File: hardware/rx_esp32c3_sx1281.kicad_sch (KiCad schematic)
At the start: 43 parts, among them U21 SX1281IMLTRT, U22 ESP32-C3FH4, U23 TLV75533PDQNR, X2 CJ17-400001010B20

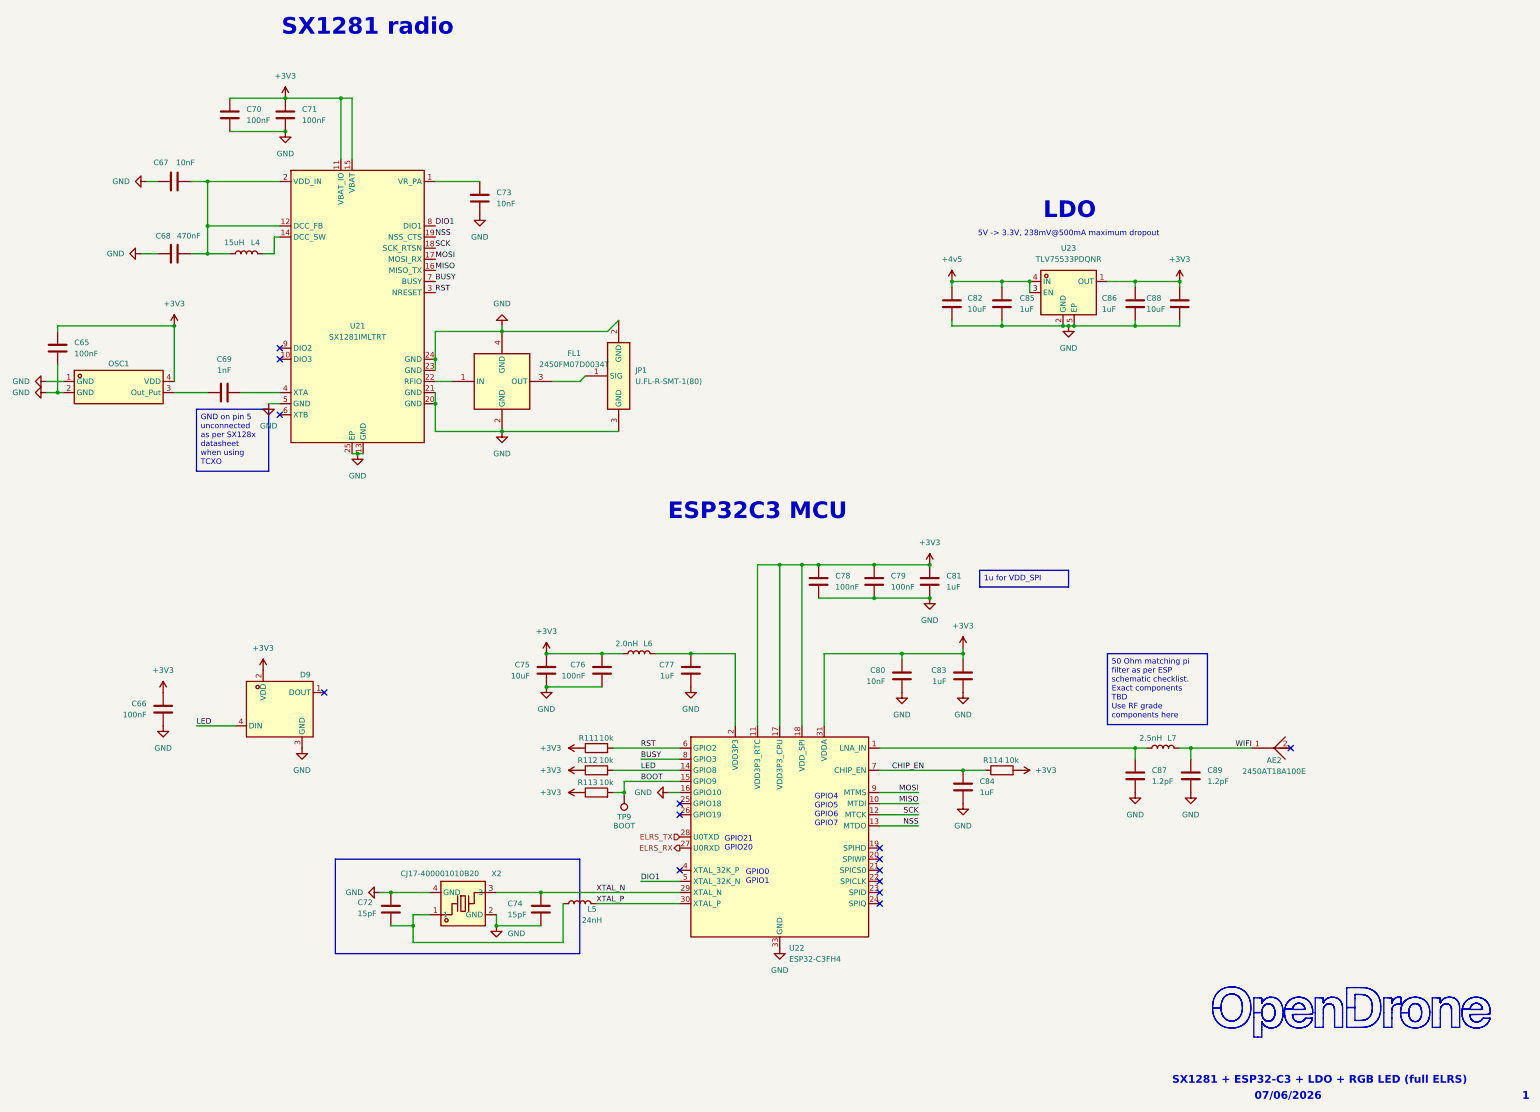
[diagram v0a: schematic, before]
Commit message: One board: merge Base and Core onto the OpenAIO-Whoop 8L HDI stackup
- hardware/OpenAIO.kicad_pcb: the routed Base and Core layouts of 8fa8d7b
  side by side in one board, all routing kept (Core promoted to 8 layers
  before the append so no Base layer was dropped). J90/J91 LGA deleted;
  their 46 nets are now direct links (51 unconnected, listed in
  research/ROUTING.md). Stackup and board setup from OpenAIO-Whoop:
  8L HDI 1+6+1, 0.997 mm, 1 oz all layers, microvia 0.25/0.10,
  buried 0.33/0.15. Base DRC severities and exclusions kept.
- hardware/OpenAIO.kicad_dru: canonical block, Whoop HDI via rules,
  Base/Core rules that still apply; LGA, 2 oz and 1.6 mm via rules gone.
- Schematic: core_interface sheet removed; DPS368 baro U28 on I2C0;
  review fixes (U3 HF cap C116, RP2354 caps C117/C118, buzzer flyback D10,
  SD card on +3.3V, D9 on +4v5, FLASH_CS -> SD_CS, PWR_FLAGs, U7 pin
  names, ESC cap pin types, L4 LCSC). ERC 32 -> 0 errors.
- Libraries project-local: every footprint, 3D model and symbol in lib;
  OPENDRONE_LIB aliases removed from the lib tables.
- Two-board projects, multiboard config and LGA tools removed; Whoop
  board tools added in hardware/tools.
- Docs: README, AGENTS.md, research/ROUTING.md (hand-over),
  SCHEMATIC-REVIEW-2026-10-15.md, Betaflight target baro.

DRC: 38 errors (25 dangling LGA escape vias, 13 Core leftovers listed),
51 unconnected (the Base-Core links), 0 net or value parity issues.

Co-Authored-By: Claude Opus 5.5 <noreply@anthropic.com>
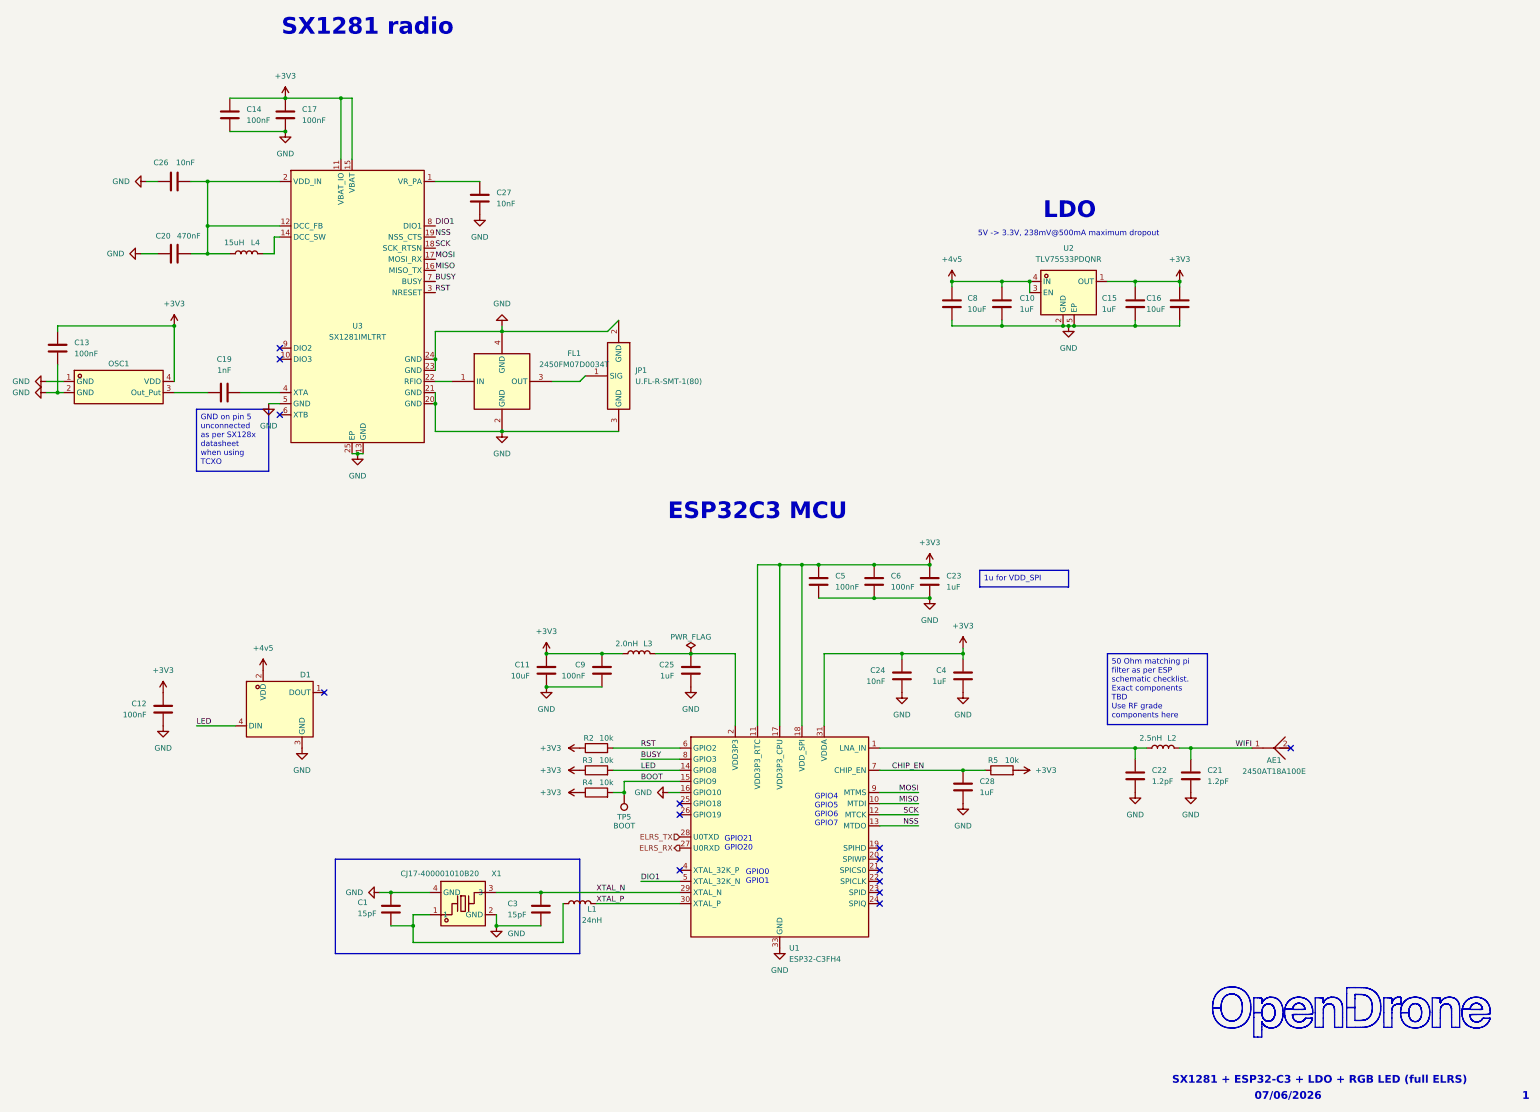
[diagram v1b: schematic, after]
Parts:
- AE1: renamed from AE2; footprint OpenRX-Shared:ANT-SMD_L3.2-W1.6 -> lib:ANT-SMD_L3.2-W1.6; symbol OpenRX-Shared:2450AT18A100E -> lib:2450AT18A100E
- C1: renamed from C72; footprint Capacitor_SMD:C_0201_0603Metric -> lib:C_0201_0603Metric
- C10: renamed from C85; footprint Capacitor_SMD:C_0201_0603Metric -> lib:C_0201_0603Metric
- C11: renamed from C75; footprint Capacitor_SMD:C_0402_1005Metric -> lib:C_0402_1005Metric
- C12: renamed from C66; footprint Capacitor_SMD:C_0201_0603Metric -> lib:C_0201_0603Metric
- C13: renamed from C65; footprint Capacitor_SMD:C_0201_0603Metric -> lib:C_0201_0603Metric
- C14: renamed from C70; footprint Capacitor_SMD:C_0201_0603Metric -> lib:C_0201_0603Metric
- C15: renamed from C86; footprint Capacitor_SMD:C_0201_0603Metric -> lib:C_0201_0603Metric
- C16: renamed from C88; footprint Capacitor_SMD:C_0402_1005Metric -> lib:C_0402_1005Metric
- C17: renamed from C71; footprint Capacitor_SMD:C_0201_0603Metric -> lib:C_0201_0603Metric
- C19: renamed from C69; footprint Capacitor_SMD:C_0201_0603Metric -> lib:C_0201_0603Metric
- C20: renamed from C68; footprint Capacitor_SMD:C_0201_0603Metric -> lib:C_0201_0603Metric
- C21: renamed from C89; footprint Capacitor_SMD:C_0201_0603Metric -> lib:C_0201_0603Metric
- C22: renamed from C87; footprint Capacitor_SMD:C_0201_0603Metric -> lib:C_0201_0603Metric
- C23: renamed from C81; footprint Capacitor_SMD:C_0201_0603Metric -> lib:C_0201_0603Metric
- C24: renamed from C80; footprint Capacitor_SMD:C_0201_0603Metric -> lib:C_0201_0603Metric
- C25: renamed from C77; footprint Capacitor_SMD:C_0201_0603Metric -> lib:C_0201_0603Metric
- C26: renamed from C67; footprint Capacitor_SMD:C_0201_0603Metric -> lib:C_0201_0603Metric
- C27: renamed from C73; footprint Capacitor_SMD:C_0201_0603Metric -> lib:C_0201_0603Metric
- C28: renamed from C84; footprint Capacitor_SMD:C_0201_0603Metric -> lib:C_0201_0603Metric
- C3: renamed from C74; footprint Capacitor_SMD:C_0201_0603Metric -> lib:C_0201_0603Metric
- C4: renamed from C83; footprint Capacitor_SMD:C_0201_0603Metric -> lib:C_0201_0603Metric
- C5: renamed from C78; footprint Capacitor_SMD:C_0201_0603Metric -> lib:C_0201_0603Metric
- C6: renamed from C79; footprint Capacitor_SMD:C_0201_0603Metric -> lib:C_0201_0603Metric
- C8: renamed from C82; footprint Capacitor_SMD:C_0402_1005Metric -> lib:C_0402_1005Metric
- C9: renamed from C76; footprint Capacitor_SMD:C_0201_0603Metric -> lib:C_0201_0603Metric
- D1: renamed from D9; footprint OpenRX-Shared:LED-SMD_4P-L1.0-W1.0-TL_XL-1010RGBC-WS2812B -> lib:LED-SMD_4P-L1.0-W1.0-TL_XL-1010RGBC-WS2812B; symbol OpenRX-Shared:XL-1010RGBC-WS2812B -> lib:XL-1010RGBC-WS2812B
- FL1: footprint OpenRX-Shared:FILTER-SMD_4P-L1.0-W0.5-L -> lib:FILTER-SMD_4P-L1.0-W0.5-L; symbol OpenRX-Shared:2450FM07D0034T -> lib:2450FM07D0034T
- JP1: footprint OpenDrone:RF-SMD_FRF05002-JSS103M -> lib:RF-SMD_FRF05002-JSS103M; symbol OpenDrone:U.FL-R-SMT-1(80) -> lib:U.FL-R-SMT-1(80)
- L1: renamed from L5; footprint Inductor_SMD:L_0201_0603Metric -> lib:L_0201_0603Metric
- L2: renamed from L7; footprint Inductor_SMD:L_0201_0603Metric -> lib:L_0201_0603Metric
- L3: renamed from L6; footprint Inductor_SMD:L_0201_0603Metric -> lib:L_0201_0603Metric
- L4: footprint Inductor_SMD:L_0805_2012Metric -> lib:L_0805_2012Metric; LCSC (none) -> C383402
- OSC1: footprint OpenRX-Shared:OSC-SMD_4P-L2.0-W1.6-BL_TXC_7Z -> lib:OSC-SMD_4P-L2.0-W1.6-BL_TXC_7Z; symbol OpenRX-Shared:OW7EL89CENUNFAYLC-52M -> lib:OW7EL89CENUNFAYLC-52M
- R2: renamed from R111; footprint Resistor_SMD:R_0201_0603Metric -> lib:R_0201_0603Metric
- R3: renamed from R112; footprint Resistor_SMD:R_0201_0603Metric -> lib:R_0201_0603Metric
- R4: renamed from R113; footprint Resistor_SMD:R_0201_0603Metric -> lib:R_0201_0603Metric
- R5: renamed from R114; footprint Resistor_SMD:R_0201_0603Metric -> lib:R_0201_0603Metric
- TP5: renamed from TP9; footprint OpenRX-Shared:SolderPad_1.2x2.0mm -> lib:SolderPad_1.2x2.0mm
- U1: renamed from U22; footprint Package_DFN_QFN:QFN-32-1EP_5x5mm_P0.5mm_EP3.7x3.7mm -> lib:QFN-32-1EP_5x5mm_P0.5mm_EP3.7x3.7mm
- U2: renamed from U23; footprint OpenRX-Shared:X2SON-4_L1.0-W1.0-P0.65-TL-EP -> lib:X2SON-4_L1.0-W1.0-P0.65-TL-EP; symbol OpenRX-Shared:TLV75533PDQNR -> lib:TLV75533PDQNR
- U3: renamed from U21; footprint OpenRX-Shared:QFN-24_L4.0-W4.0-P0.50-TL-EP2.6 -> lib:QFN-24_L4.0-W4.0-P0.50-TL-EP2.6; symbol OpenRX-Shared:SX1281IMLTRT -> lib:SX1281IMLTRT
- X1: renamed from X2; footprint OpenRX-Shared:CRYSTAL-SMD_4P-L1.6-W1.2-BL -> lib:CRYSTAL-SMD_4P-L1.6-W1.2-BL; symbol OpenRX-Shared:CJ17-400001010B20 -> lib:CJ17-400001010B20
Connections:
- net +3V3: no longer D1.2 (VDD)
- net +4v5: now also D1.2 (VDD)
